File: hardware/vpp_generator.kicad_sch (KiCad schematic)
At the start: 17 parts, among them Q5 TIP120, Q6 BC327, U2 74LS06N

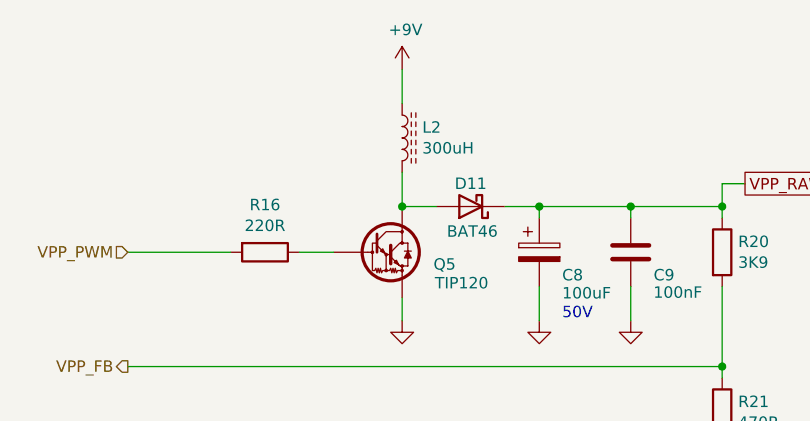
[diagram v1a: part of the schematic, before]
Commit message: Rev.G. Change external power supply to a MT3606 DC-DC Module
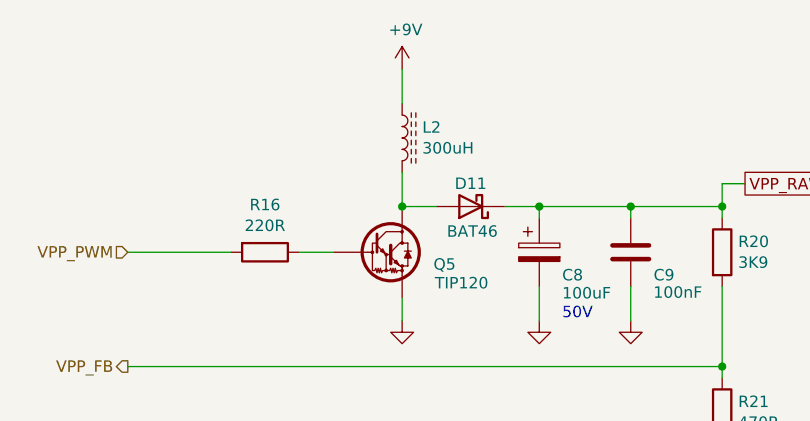
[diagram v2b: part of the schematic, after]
